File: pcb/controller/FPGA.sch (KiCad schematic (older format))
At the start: 22 parts, among them J3001 Conn_01x06_Male, J3002 Conn_01x04_Male, U3001 XC7S25-L1FTGB196, U3002 S25FL127SABN, U3003 74AVC4TD245BQ

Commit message: controller layout done and schematic reviewed
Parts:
- added R3014, R3015: 4.7K, Resistor_SMD:R_0402_1005Metric, symbol Device:R
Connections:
- net +3V3D: now also R3014.1, R3015.1
- net ADC_MODE: now also U3001.M2 (IO_L19N_T3_VREF_34); no longer U3001.M1 (IO_L18P_T2_34)
- net at J3001.4 (Pin_4), U3003.12 (B3): now also R3015.2
- net at J3001.2 (Pin_2), U3003.14 (B1): now also R3014.2
- net RELAY_B: now reaches U3001.H2 (IO_L14P_T2_SRCC_34)
- net RELAY_A: now reaches U3001.J1 (IO_L15N_T2_DQS_34)
- net RS485-D: now reaches U3001.J2 (IO_L15P_T2_DQS_34)
- net RS485-DE: now reaches U3001.L1 (IO_L18N_T2_34)
- net RS485-RE: now reaches U3001.L2 (IO_L22N_T3_34)
- new net RS485-R: U3001.M1 (IO_L18P_T2_34)
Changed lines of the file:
@@
 $EndComp
 Wire Wire Line
-	10050 4050 10750 4050
+	10050 4050 10100 4050
 Wire Wire Line
 	10050 4150 10750 4150
 Wire Wire Line
-	10050 4250 10750 4250
+	10050 4250 10400 4250
 Wire Wire Line
 	10050 4350 10750 4350
@@
 Text GLabel 9100 4950 0    50   Input ~ 0
 +3V3D
-Text GLabel 10650 3800 0    50   Input ~ 0
+Text GLabel 10650 3800 2    50   Input ~ 0
 +3V3D
 Text GLabel 9800 2750 0    50   Input ~ 0
@@
 FIBER_RX
 Wire Wire Line
-	8000 4350 8100 4350
+	8000 4650 8100 4650
 Wire Wire Line
 	9200 1800 9100 1800
@@
 	9100 2100 9100 2200
 $Comp
-L power:GND #PWR?
+L power:GND #PWR0136
 U 1 1 5C4ECF97
 P 9100 2200
-F 0 "#PWR?" H 9100 1950 50  0001 C CNN
+F 0 "#PWR0136" H 9100 1950 50  0001 C CNN
 F 1 "GND" H 9105 2027 50  0000 C CNN
 F 2 "" H 9100 2200 50  0001 C CNN
@@
 Text GLabel 8100 4850 2    50   Input ~ 0
 ADC_SDIO
-Text GLabel 8100 4350 2    50   Input ~ 0
+Text GLabel 8100 4650 2    50   Input ~ 0
 ADC_MODE
 Wire Wire Line
@@
 Text Label 5400 4250 0    50   ~ 0
 LED2
+Wire Wire Line
+	8000 4350 8100 4350
+Text GLabel 8100 4350 2    50   Input ~ 0
+RS485-R
+Wire Wire Line
+	8000 5250 8100 5250
+Text GLabel 8100 5250 2    50   Input ~ 0
+RS485-RE
+Wire Wire Line
+	8000 4450 8100 4450
+Text GLabel 8100 4450 2    50   Input ~ 0
+RS485-DE
+Wire Wire Line
+	8000 3750 8100 3750
+Text GLabel 8100 3750 2    50   Input ~ 0
+RS485-D
+Wire Wire Line
+	8000 3850 8100 3850
+Text GLabel 8100 3850 2    50   Input ~ 0
+RELAY_A
+Wire Wire Line
+	8000 3550 8100 3550
+Text GLabel 8100 3550 2    50   Input ~ 0
+RELAY_B
+$Comp
+L Device:R R3014
+U 1 1 5C4BCB93
+P 10100 3750
+F 0 "R3014" H 10170 3796 50  0000 L CNN
+F 1 "4.7K" H 10170 3705 50  0000 L CNN
+F 2 "Resistor_SMD:R_0402_1005Metric" V 10030 3750 50  0001 C CNN
+F 3 "~" H 10100 3750 50  0001 C CNN
+	1    10100 3750
+	1    0    0    -1
+$EndComp
+Wire Wire Line
+	10100 3900 10100 4050
+Connection ~ 10100 4050
+Wire Wire Line
+	10100 4050 10750 4050
+Text GLabel 10400 3550 2    50   Input ~ 0
++3V3D
+Wire Wire Line
+	10100 3600 10100 3550
+$Comp
+L Device:R R3015
+U 1 1 5C4CAE4D
+P 10400 3800
+F 0 "R3015" H 10470 3846 50  0000 L CNN
+F 1 "4.7K" H 10470 3755 50  0000 L CNN
+F 2 "Resistor_SMD:R_0402_1005Metric" V 10330 3800 50  0001 C CNN
+F 3 "~" H 10400 3800 50  0001 C CNN
+	1    10400 3800
+	1    0    0    -1
+$EndComp
+Wire Wire Line
+	10400 3950 10400 4250
+Connection ~ 10400 4250
+Wire Wire Line
+	10400 4250 10750 4250
+Wire Wire Line
+	10400 3650 10400 3550
+Wire Wire Line
+	10100 3550 10400 3550
 $EndSCHEMATC

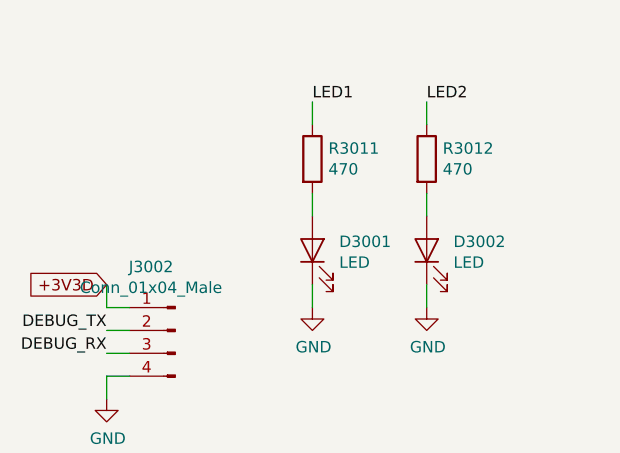
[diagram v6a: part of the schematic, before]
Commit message: updated schematic component values
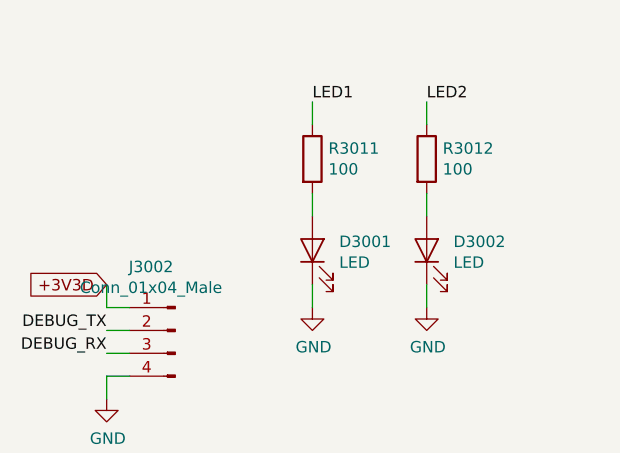
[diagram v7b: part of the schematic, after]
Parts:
- R3011, R3012: value 470 -> 100
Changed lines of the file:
@@
 P 10500 1150
 F 0 "R3012" H 10570 1196 50  0000 L CNN
-F 1 "470" H 10570 1105 50  0000 L CNN
+F 1 "100" H 10570 1105 50  0000 L CNN
 F 2 "Resistor_SMD:R_0402_1005Metric" V 10430 1150 50  0001 C CNN
 F 3 "~" H 10500 1150 50  0001 C CNN
@@
 P 10000 1150
 F 0 "R3011" H 10070 1196 50  0000 L CNN
-F 1 "470" H 10070 1105 50  0000 L CNN
+F 1 "100" H 10070 1105 50  0000 L CNN
 F 2 "Resistor_SMD:R_0402_1005Metric" V 9930 1150 50  0001 C CNN
 F 3 "~" H 10000 1150 50  0001 C CNN
